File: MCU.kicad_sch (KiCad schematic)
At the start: 24 parts, among them U2 Si7021-A20, Y1 39MHz 10pF

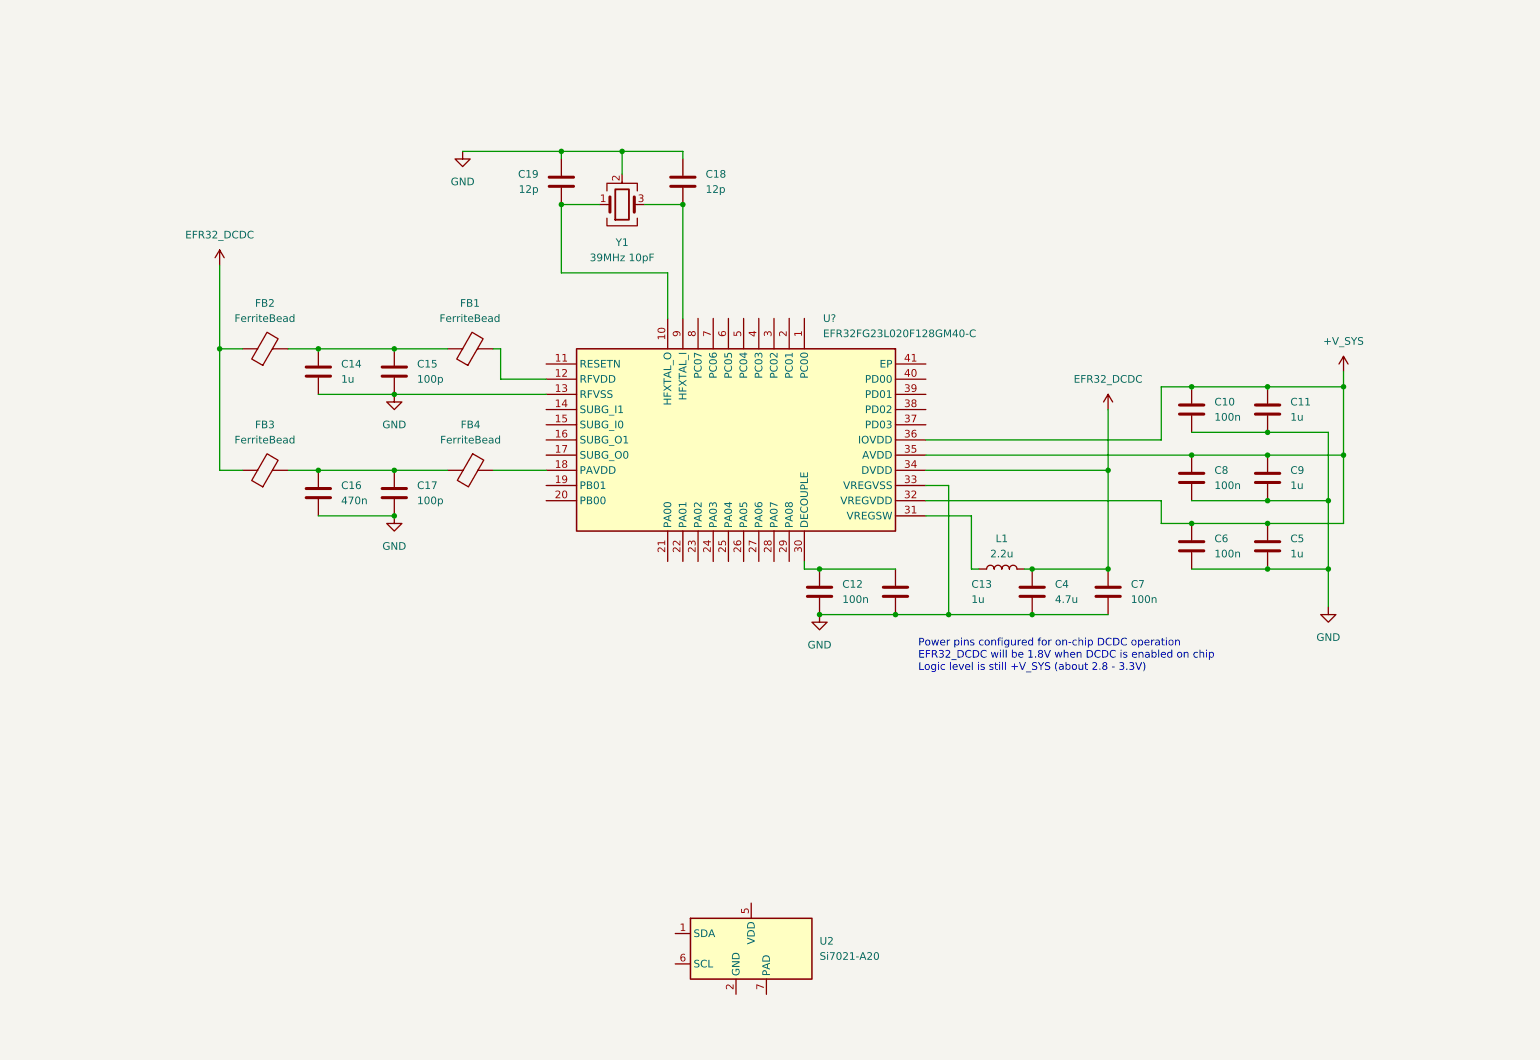
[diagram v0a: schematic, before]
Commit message: debug connector and buttons
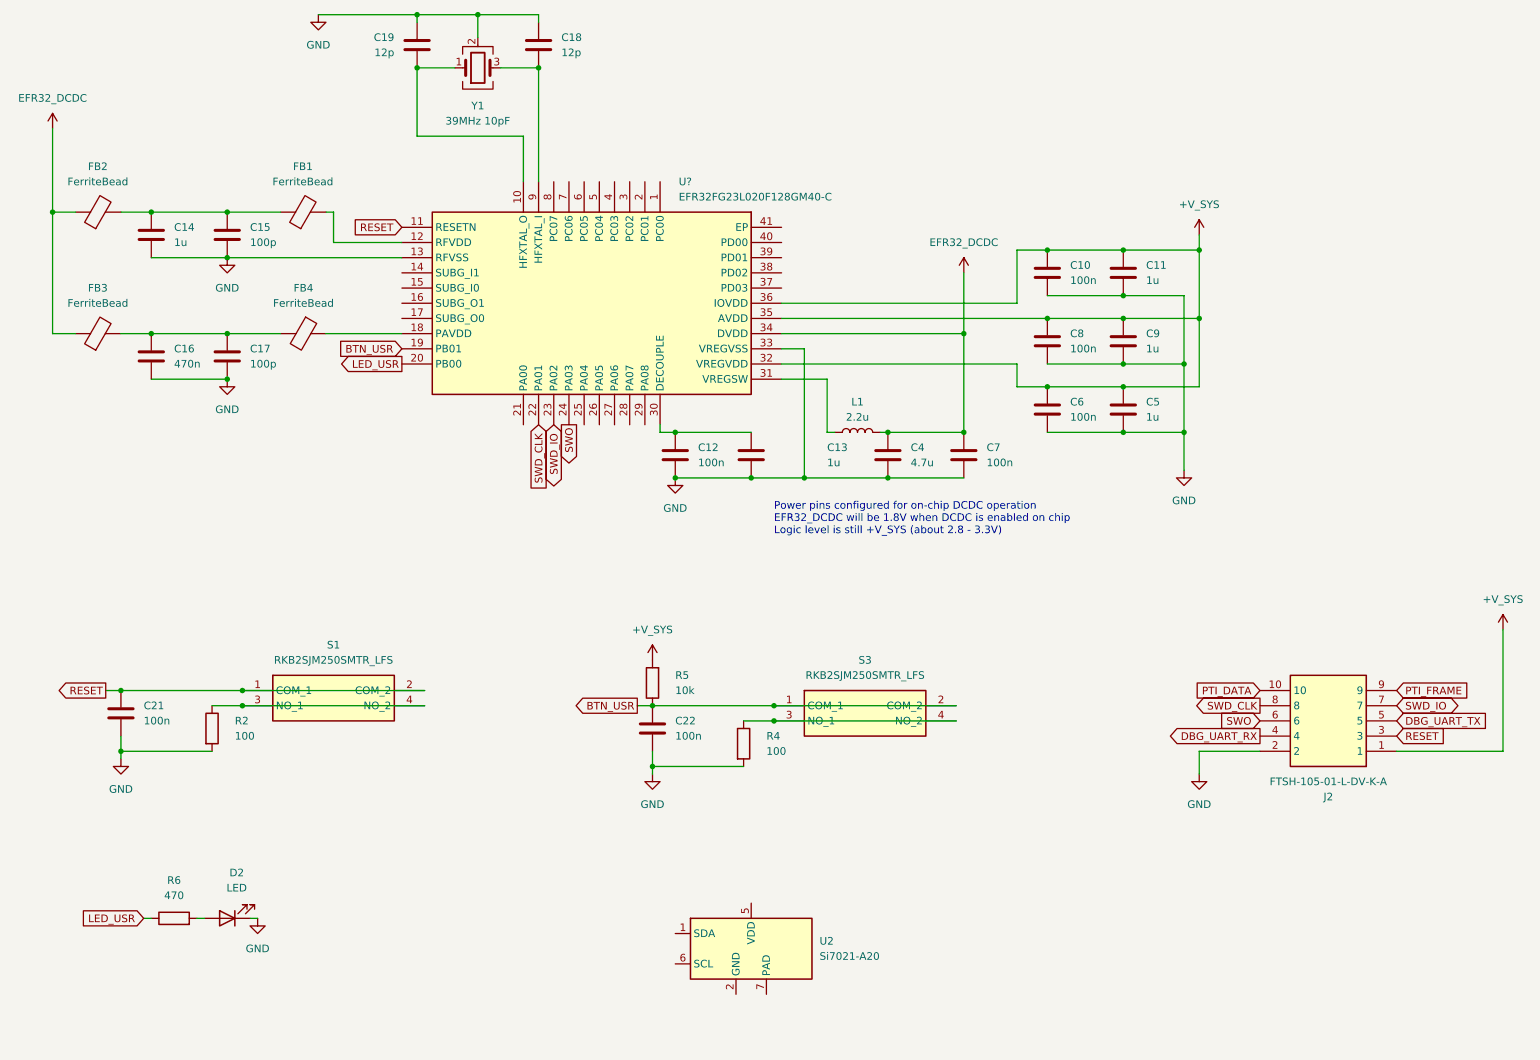
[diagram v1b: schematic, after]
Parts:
- added C21, C22: 100n, Capacitor_SMD:C_0603_1608Metric_Pad1.08x0.95mm_HandSolder, symbol Device:C
- added D2: LED, LED_SMD:LED_0603_1608Metric_Pad1.05x0.95mm_HandSolder, symbol Device:LED
- added J2: FTSH-105-01-L-DV-K-A, SamacSys_Parts:FTSH-105-XX-YYY-DV-K-A, symbol SamacSys_Parts:FTSH-105-01-L-DV-K-A
- added R2, R4: 100, Resistor_SMD:R_0603_1608Metric_Pad0.98x0.95mm_HandSolder, symbol Device:R
- added R5: 10k, Resistor_SMD:R_0603_1608Metric_Pad0.98x0.95mm_HandSolder, symbol Device:R
- added R6: 470, Resistor_SMD:R_0603_1608Metric_Pad0.98x0.95mm_HandSolder, symbol Device:R
- added S1, S3: RKB2SJM250SMTR_LFS, RKB2SJM250SMTRLFS, symbol SamacSys_Parts:RKB2SJM250SMTR_LFS
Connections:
- net +V_SYS: now also J2.1, R5.2
- net GND: now also C21.2, C22.2, D2.1 (K), J2.2, R2.2, R4.2
- net RESET: now reaches U?.11 (RESETN)
- net RESET: now also C21.1, J2.3, S1.1 (COM_1), S1.2 (COM_2)
- net BTN_USR: now reaches U?.19 (PB01)
- net BTN_USR: now also C22.1, R5.1, S3.1 (COM_1), S3.2 (COM_2)
- net LED_USR: now reaches U?.20 (PB00)
- net LED_USR: now also R6.1
- net SWD_CLK: now reaches U?.22 (PA01)
- net SWD_CLK: now also J2.8
- net SWD_IO: now reaches U?.23 (PA02)
- net SWD_IO: now also J2.7
- net SWO: now reaches U?.24 (PA03)
- net SWO: now also J2.6
- new net: R4.1, S3.3 (NO_1), S3.4 (NO_2)
- new net: D2.2 (A), R6.2
- new net: R2.1, S1.3 (NO_1), S1.4 (NO_2)
- new net DBG_UART_RX: J2.4
- new net DBG_UART_TX: J2.5
- new net PTI_DATA: J2.10
- new net PTI_FRAME: J2.9
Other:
- moved on the sheet: C10, C11, C12, C13, C14, C15, C16, C17, C18, C19, C4, C5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

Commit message: add backscatter and active radio components
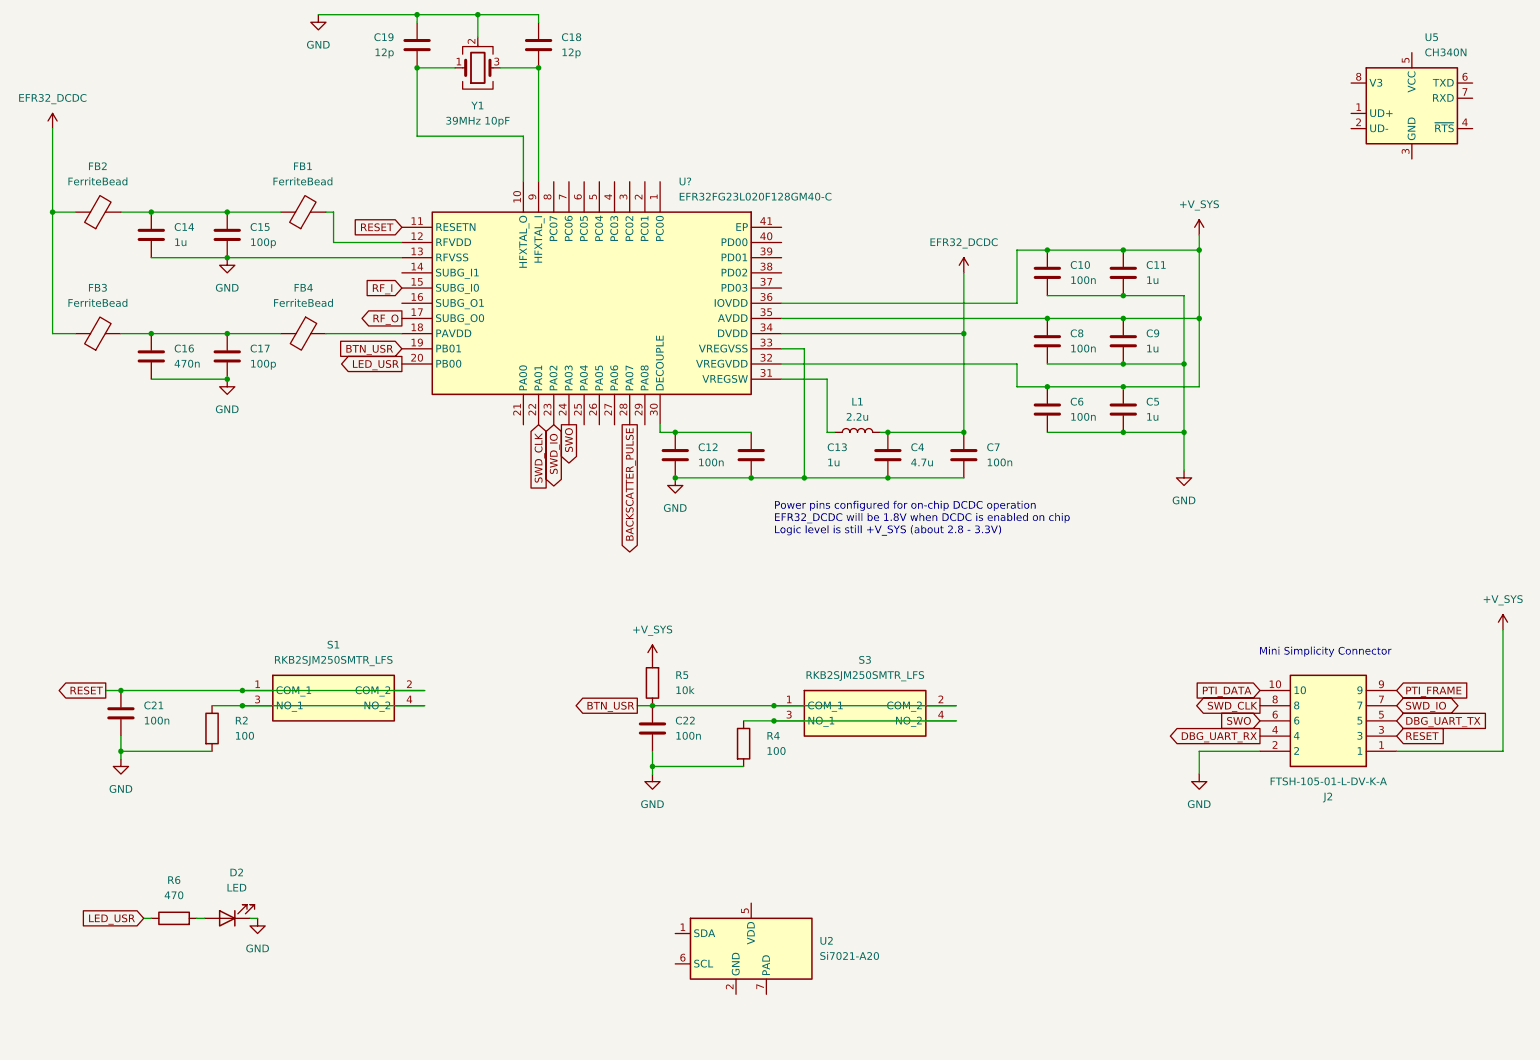
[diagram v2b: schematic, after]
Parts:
- added U5: CH340N, Package_SO:JEITA_SOIC-8_3.9x4.9mm_P1.27mm, symbol Interface_USB:CH340N
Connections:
- net RF_I: now reaches U?.15 (SUBG_I0)
- net RF_O: now reaches U?.17 (SUBG_O0)
- net BACKSCATTER_PULSE: now reaches U?.28 (PA07)
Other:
- note added: "Mini Simplicity Connector"
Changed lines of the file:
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@@
 		)
 	)
+	(text "Mini Simplicity Connector"
+		(exclude_from_sim no)
+		(at 240.792 130.81 0)
+		(effects
+			(font
+				(size 1.27 1.27)
+			)
+		)
+	)
 	(junction
 		(at 217.17 82.55)
@@
 		)
 	)
+	(global_label "BACKSCATTER_PULSE"
+		(shape output)
+		(at 124.46 92.71 270)
+		(fields_autoplaced yes)
+		(effects
+			(font
+				(size 1.27 1.27)
+			)
+			(justify right)
+		)
+		(property "Intersheetrefs" "${INTERSHEET_REFS}"
+			(at 124.46 115.4708 90)
+			(hide yes)
+			(show_name no)
+			(do_not_autoplace no)
+			(effects
+				(font
+					(size 1.27 1.27)
+				)
+				(justify right)
+			)
+		)
+	)
 	(global_label "SWO"
 		(shape output)
@@
 		)
 	)
+	(global_label "RF_O"
+		(shape output)
+		(at 86.36 74.93 180)
+		(fields_autoplaced yes)
+		(effects
+			(font
+				(size 1.27 1.27)
+			)
+			(justify right)
+		)
+		(property "Intersheetrefs" "${INTERSHEET_REFS}"
+			(at 78.7181 74.93 0)
+			(hide yes)
+			(show_name no)
+			(do_not_autoplace no)
+			(effects
+				(font
+					(size 1.27 1.27)
+				)
+				(justify right)
+			)
+		)
+	)
+	(global_label "RF_I"
+		(shape input)
+		(at 86.36 69.85 180)
+		(fields_autoplaced yes)
+		(effects
+			(font
+				(size 1.27 1.27)
+			)
+			(justify right)
+		)
+		(property "Intersheetrefs" "${INTERSHEET_REFS}"
+			(at 79.4438 69.85 0)
+			(hide yes)
+			(show_name no)
+			(do_not_autoplace no)
+			(effects
+				(font
+					(size 1.27 1.27)
+				)
+				(justify right)
+			)
+		)
+	)
 	(global_label "LED_USR"
 		(shape input)
@@
 					(unit 1)
 				)
+			)
+		)
+	)
+	(symbol
+		(lib_id "Interface_USB:CH340N")
+		(at 255.27 38.1 0)
+		(unit 1)
+		(body_style 1)
+		(exclude_from_sim no)
+		(in_bom yes)
+		(on_board yes)
+		(in_pos_files yes)
+		(dnp no)
+		(fields_autoplaced yes)
+		(property "Reference" "U5"
+			(at 257.4133 27.94 0)
+			(show_name no)
+			(do_not_autoplace no)
+			(effects
+				(font
+					(size 1.27 1.27)
+				)
+				(justify left)
+			)
+		)
+		(property "Value" "CH340N"
+			(at 257.4133 30.48 0)
+			(show_name no)
+			(do_not_autoplace no)
+			(effects
+				(font
+					(size 1.27 1.27)
+				)
+				(justify left)
+			)
+		)
+		(property "Footprint" "Package_SO:JEITA_SOIC-8_3.9x4.9mm_P1.27mm"
+			(at 251.46 19.05 0)
+			(hide yes)
+			(show_name no)
+			(do_not_autoplace no)
+			(effects
+				(font
+					(size 1.27 1.27)
+				)
+			)
+		)
+		(property "Datasheet" "https://aitendo3.sakura.ne.jp/aitendo_data/product_img/ic/inteface/CH340N/ch340n.pdf"
+			(at 252.73 33.02 0)
+			(hide yes)
+			(show_name no)
+			(do_not_autoplace no)
+			(effects
+				(font
+					(size 1.27 1.27)
+				)
+			)
+		)
+		(property "Description" "USB serial converter, 2Mbps, UART, JEITA SOIC-8 (SOP-8)"
+			(at 255.27 38.1 0)
+			(hide yes)
+			(show_name no)
+			(do_not_autoplace no)
+			(effects
+				(font
+					(size 1.27 1.27)
+				)
+			)
+		)
+		(pin "4"
+		)
+		(pin "8"
+		)
+		(pin "1"
+		)
+		(pin "5"
+		)
+		(pin "6"
+		)
+		(pin "2"
+		)
+		(pin "7"
+		)
+		(pin "3"
+		)
+		(instances
+			(project "WINLAB-LP-Radio-Sensor-Hub"
+				(path "/0de7ee4a-bb98-4bc6-bb89-3afafc4b94b5/f02c211f-c559-4db5-8225-ca108efc3892"
+					(reference "U5")
+					(unit 1)
+				)

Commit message: add initial pinouts and USB
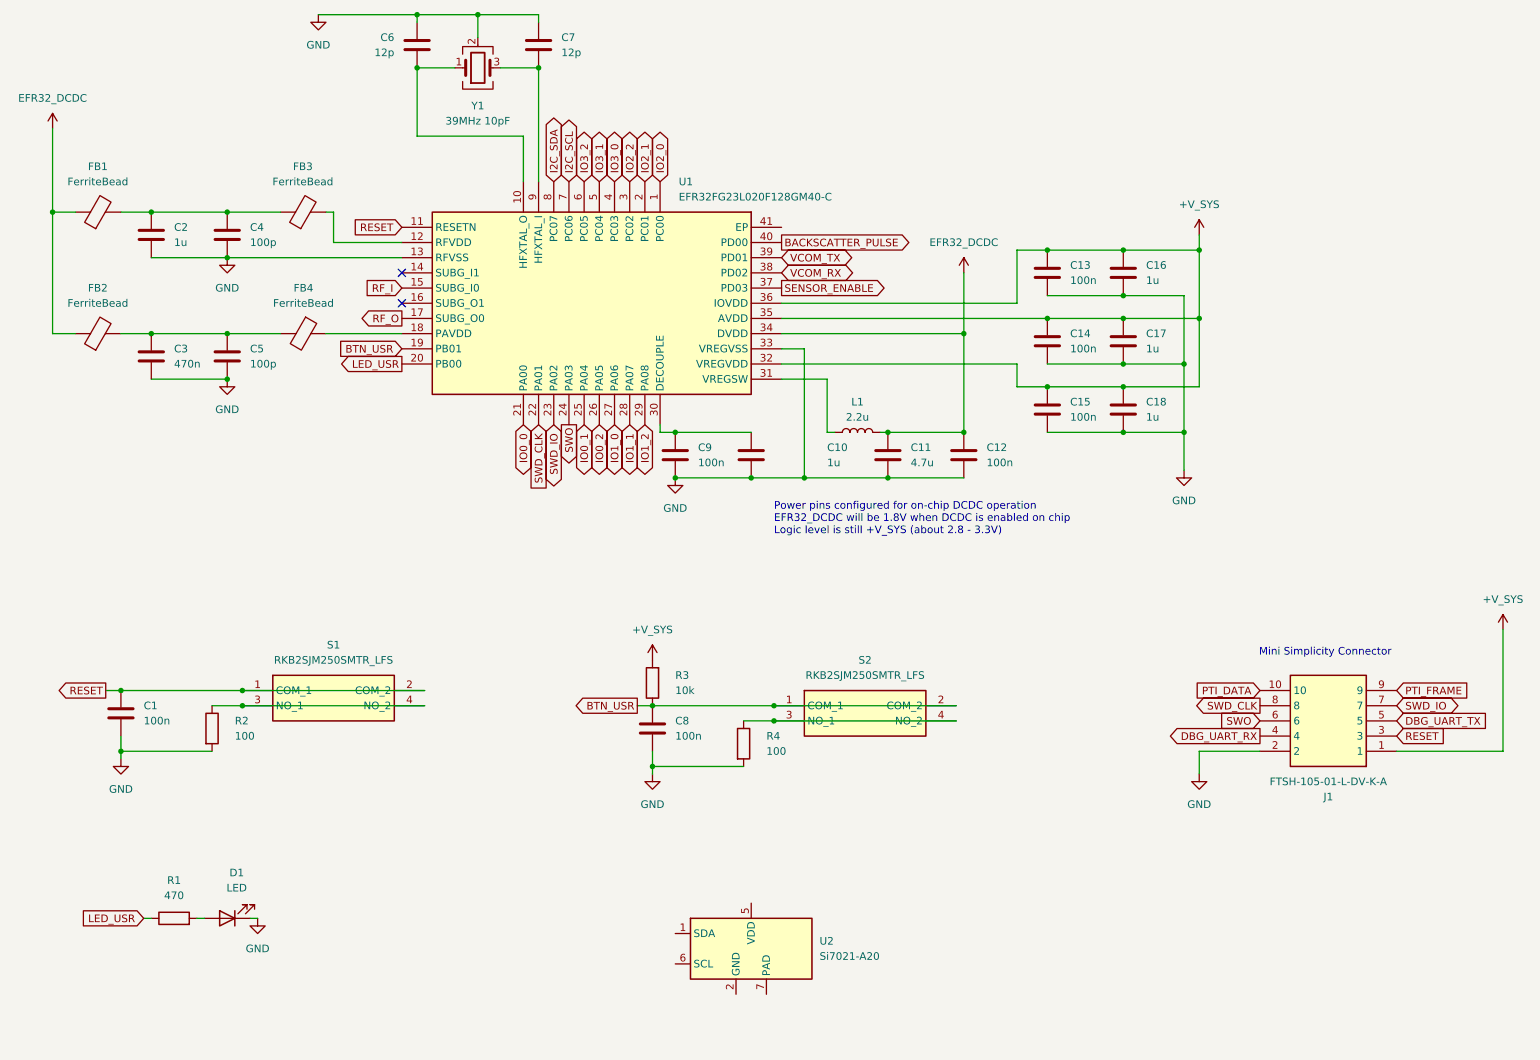
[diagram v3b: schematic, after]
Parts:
- removed U5: CH340N, Package_SO:JEITA_SOIC-8_3.9x4.9mm_P1.27mm, symbol Interface_USB:CH340N
- gave numbers to parts that had none: 1
- renumbered C21 to C1, C13 to C10, C4 to C11, C7 to C12, C10 to C13, C8 to C14, C6 to C15, C11 to C16, C9 to C17, C5 to C18, C14 to C2, C16 to C3, C15 to C4, C17 to C5, C19 to C6, C18 to C7, C22 to C8, C12 to C9, D2 to D1, FB2 to FB1, FB3 to FB2, FB1 to FB3, J2 to J1, R6 to R1, R5 to R3, S3 to S2
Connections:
- net BACKSCATTER_PULSE: now also U1.40 (PD00); no longer U1.28 (PA07)
- net IO2_0: now reaches U1.1 (PC00)
- net IO2_1: now reaches U1.2 (PC01)
- net IO0_0: now reaches U1.21 (PA00)
- net IO0_1: now reaches U1.25 (PA04)
- net IO0_2: now reaches U1.26 (PA05)
- net IO1_0: now reaches U1.27 (PA06)
- net IO1_2: now reaches U1.29 (PA08)
- net IO2_2: now reaches U1.3 (PC02)
- net SENSOR_ENABLE: now reaches U1.37 (PD03)
- net VCOM_RX: now reaches U1.38 (PD02)
- net VCOM_TX: now reaches U1.39 (PD01)
- net IO3_0: now reaches U1.4 (PC03)
- net IO3_1: now reaches U1.5 (PC04)
- net IO3_2: now reaches U1.6 (PC05)
- net I2C_SCL: now reaches U1.7 (PC06)
- net I2C_SDA: now reaches U1.8 (PC07)
- new net IO1_1: U1.28 (PA07)
- no-connect marks 0 -> 2

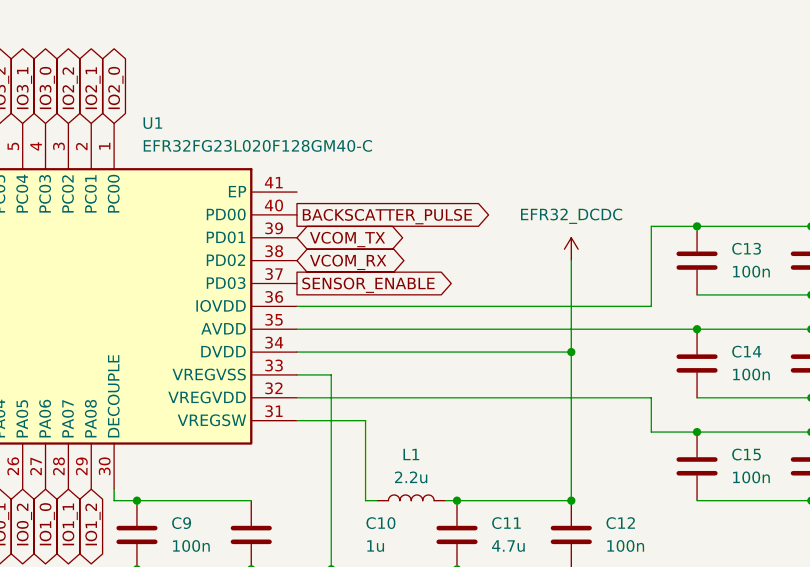
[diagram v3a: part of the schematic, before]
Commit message: add IO ports, begin layout
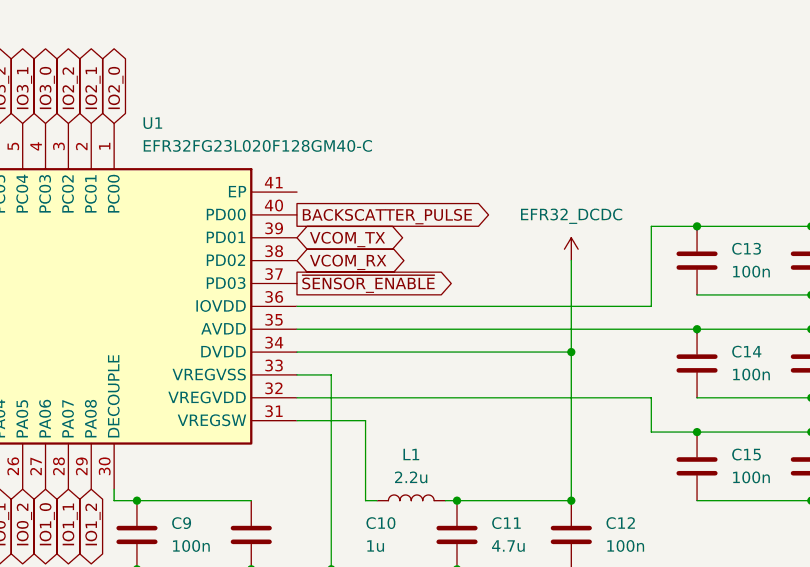
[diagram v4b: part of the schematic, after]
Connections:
- net SENSOR_ENABLE renamed ~{SENSOR_ENABLE}
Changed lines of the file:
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@@
 		)
 	)
-	(global_label "SENSOR_ENABLE"
+	(global_label "~{SENSOR_ENABLE}"
 		(shape output)
 		(at 149.86 69.85 0)

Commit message: minor schematic changes
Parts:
- added C29: 100n, Capacitor_SMD:C_0603_1608Metric_Pad1.08x0.95mm_HandSolder, symbol Device:C
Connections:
- net +V_SYS: now also U2.5 (VDD), C29.1
- net GND: now also U1.41 (EP), U2.2 (GND), U2.7 (PAD), C29.2
- net I2C_SCL: now also U2.6 (SCL)
- net I2C_SDA: now also U2.1 (SDA)
